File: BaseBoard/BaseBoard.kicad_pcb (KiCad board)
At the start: 4 copper layers, 50 x 35 mm, 57 parts, among them J1 locked, J2 Serial Port, J3 base connector, Q1 PMN48XP, Q2 SSM6L820R, SW1 Battery switch, SW2 boot, SW3 Reset, U1 ESP32-WROOM-E, U3 MCP73831-2ACI-OT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

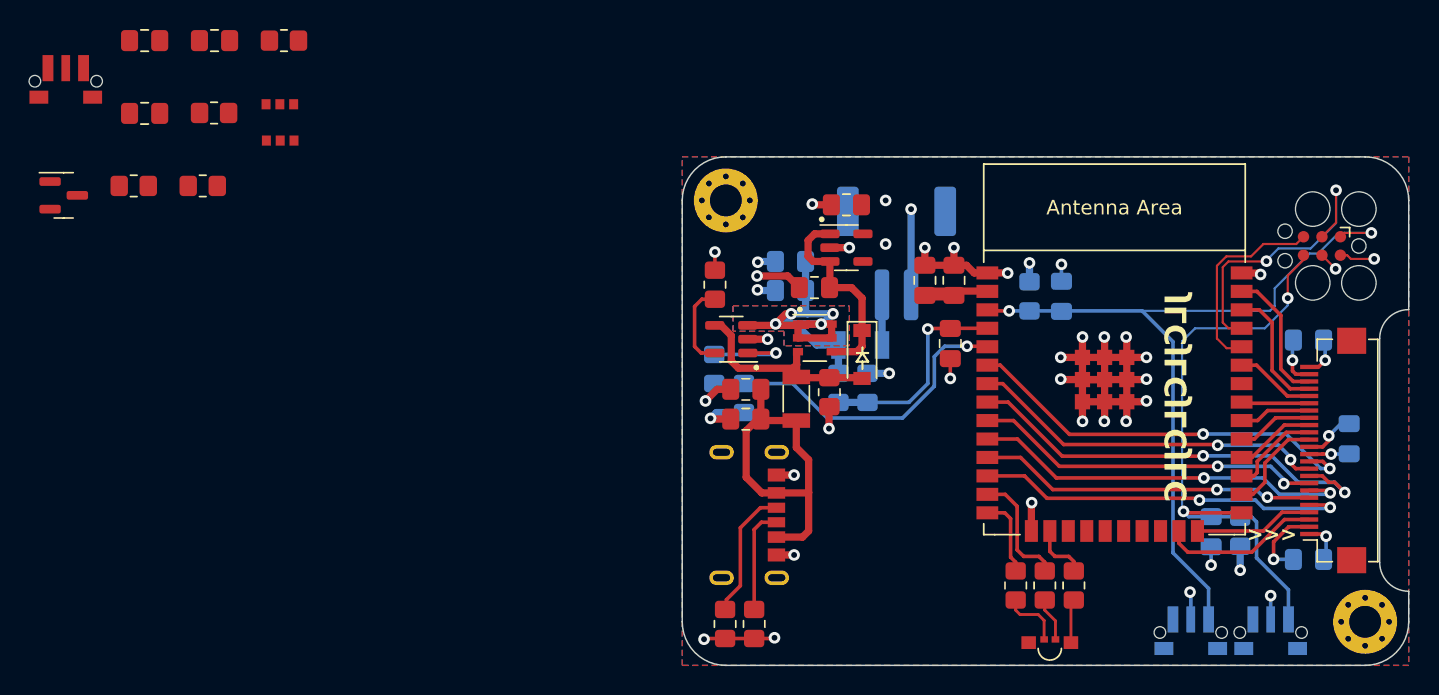
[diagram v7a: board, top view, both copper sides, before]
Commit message: Routes new power latch circuit
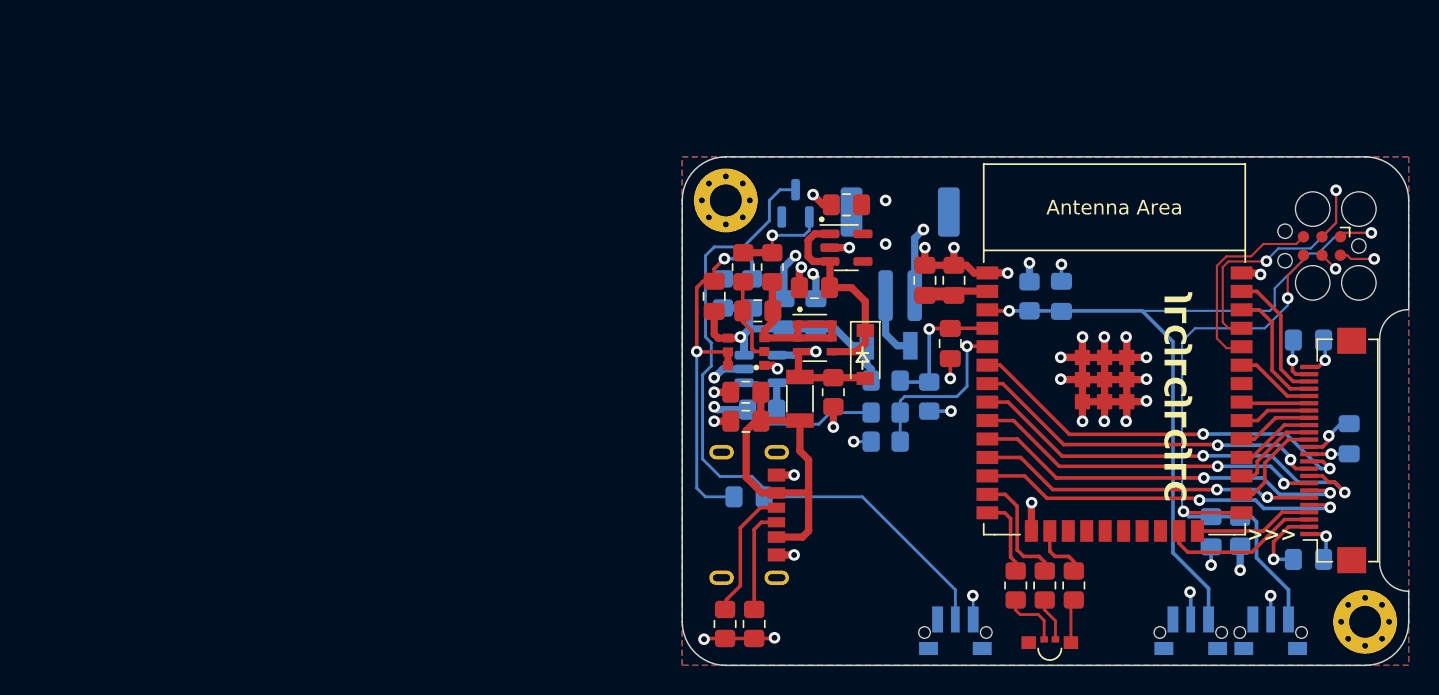
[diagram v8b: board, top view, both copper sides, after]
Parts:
- C8, D3, R14, R15, R8, SW1, U3: moved to B.Cu
- moved SW1 72.0 mm to (138.8, 111.8), turned to 180 degrees
- moved C8 52.1 mm to (124.6, 103.4), turned to 180 degrees
- moved D3 50.4 mm to (127.8, 83.2), turned to 90 degrees
- moved C17 44.3 mm to (125.2, 90.6)
- moved R14 41.2 mm to (122.8, 89.4), turned to 90 degrees
- moved R15 39.0 mm to (124.8, 89.4), turned to 90 degrees
- moved C12 38.6 mm to (122.2, 89.6), turned to 90 degrees
- moved R16 37.6 mm to (124.2, 87.6), turned to 90 degrees
- moved R17 37.1 mm to (126.2, 87.6), turned to -90 degrees
- moved Q2 35.7 mm to (124.4, 93.4), turned to 90 degrees
- moved R9 12.2 mm to (134.0, 97.6), turned to 0 degrees
- moved R13 10.2 mm to (134.0, 99.6), turned to 180 degrees
- moved R8 9.19 mm to (125.5, 97.4), turned to 180 degrees
- moved R6 4.29 mm to (137.0, 96.5), turned to -90 degrees
- moved C14 4.00 mm to (129.2, 90.8), turned to 90 degrees
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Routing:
- net Net-(D3-K): track 0.00 -> 48.0 mm
- net Net-(Q2A-D): track 0.00 -> 26.1 mm, vias 0 -> 2
- net +SWITCHED_BATT: track 0.00 -> 13.0 mm
- net BAT_STAT: track 23.0 -> 12.0 mm
- net +BATT: track 30.0 -> 22.3 mm, vias 4 -> 1
- net Net-(D3-A): track 0.00 -> 6.81 mm, vias 0 -> 1
- net Net-(Q2A-G): track 0.00 -> 5.81 mm
- net Net-(U3-STAT): track 6.23 -> 11.5 mm, vias 1 -> 0
- net BAT_SENSE: track 14.6 -> 9.71 mm
- net Net-(U3-PROG): track 5.93 -> 1.87 mm
- net +5V: track 14.3 -> 10.3 mm, vias 0 -> 1
- net GND: track 100.1 -> 102.2 mm, vias 41 -> 44
- net Net-(BT1-+): track 3.45 -> 4.68 mm
- removed copper zone on B.Cu, net +BATT
- removed copper zone on F.Cu, net +BATT
